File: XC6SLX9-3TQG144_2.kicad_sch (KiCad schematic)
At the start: 28 parts, among them U1 XC6SLX9-3TQG144

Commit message: updated design - still needs vcc routing
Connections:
- net GND: now also U1.108 (GND), U1.113 (GND), U1.13 (GND), U1.130 (GND), U1.136 (GND), U1.25 (GND), U1.3 (GND), U1.49 (GND), U1.54 (GND), U1.68 (GND), U1.73 (SUSPEND), U1.77 (GND), U1.91 (GND), U1.96 (GND); no longer U1.P108 (GND), U1.P113 (GND), U1.P13 (GND), U1.P130 (GND), U1.P136 (GND), U1.P25 (GND), U1.P3 (GND), U1.P49 (GND), U1.P54 (GND), U1.P68 (GND), U1.P73 (SUSPEND), U1.P77 (GND), U1.P91 (GND), U1.P96 (GND)
- net SHUNTL: now also U1.128 (VCCINT), U1.19 (VCCINT), U1.28 (VCCINT), U1.52 (VCCINT), U1.89 (VCCINT); no longer U1.P128 (VCCINT), U1.P19 (VCCINT), U1.P28 (VCCINT), U1.P52 (VCCINT), U1.P89 (VCCINT)
- net TCK: now also U1.109 (TCK); no longer U1.P109 (TCK)
- net TDI: now also U1.110 (TDI); no longer U1.P110 (TDI)
- net TDO: now also U1.106 (TDO); no longer U1.P106 (TDO)
- net TMS: now also U1.107 (TMS); no longer U1.P107 (TMS)
- net VCC: now also U1.103 (VCCO_1), U1.122 (VCCO_0), U1.125 (VCCO_0), U1.129 (VCCAUX), U1.135 (VCCO_0), U1.18 (VCCO_3), U1.20 (VCCAUX), U1.31 (VCCO_3), U1.36 (VCCAUX), U1.4 (VCCO_3), U1.42 (VCCO_2), U1.53 (VCCAUX), U1.63 (VCCO_2), U1.76 (VCCO_1), U1.86 (VCCO_1), U1.90 (VCCAUX); no longer U1.P103 (VCCO_1), U1.P122 (VCCO_0), U1.P125 (VCCO_0), U1.P129 (VCCAUX), U1.P135 (VCCO_0), U1.P18 (VCCO_3), U1.P20 (VCCAUX), U1.P31 (VCCO_3), U1.P36 (VCCAUX), U1.P4 (VCCO_3), U1.P42 (VCCO_2), U1.P53 (VCCAUX), U1.P63 (VCCO_2), U1.P76 (VCCO_1), U1.P86 (VCCO_1), U1.P90 (VCCAUX)
- net at R4.1, SJ2.2: now also U1.37 (PROGRAM_B_2); no longer U1.P37 (PROGRAM_B_2)
- net at D1.1, R5.1, SJ1.2: now also U1.71 (DONE_2); no longer U1.P71 (DONE_2)

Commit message: updated schematic and pcb, fixed silkscreen - Ready for review
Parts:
- renumbered SJ1 to JP1, SJ2 to JP2
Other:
- moved on the sheet: C1, C13, C14, C15, C16, C18, C19, C2, C20, C21, C3, C4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

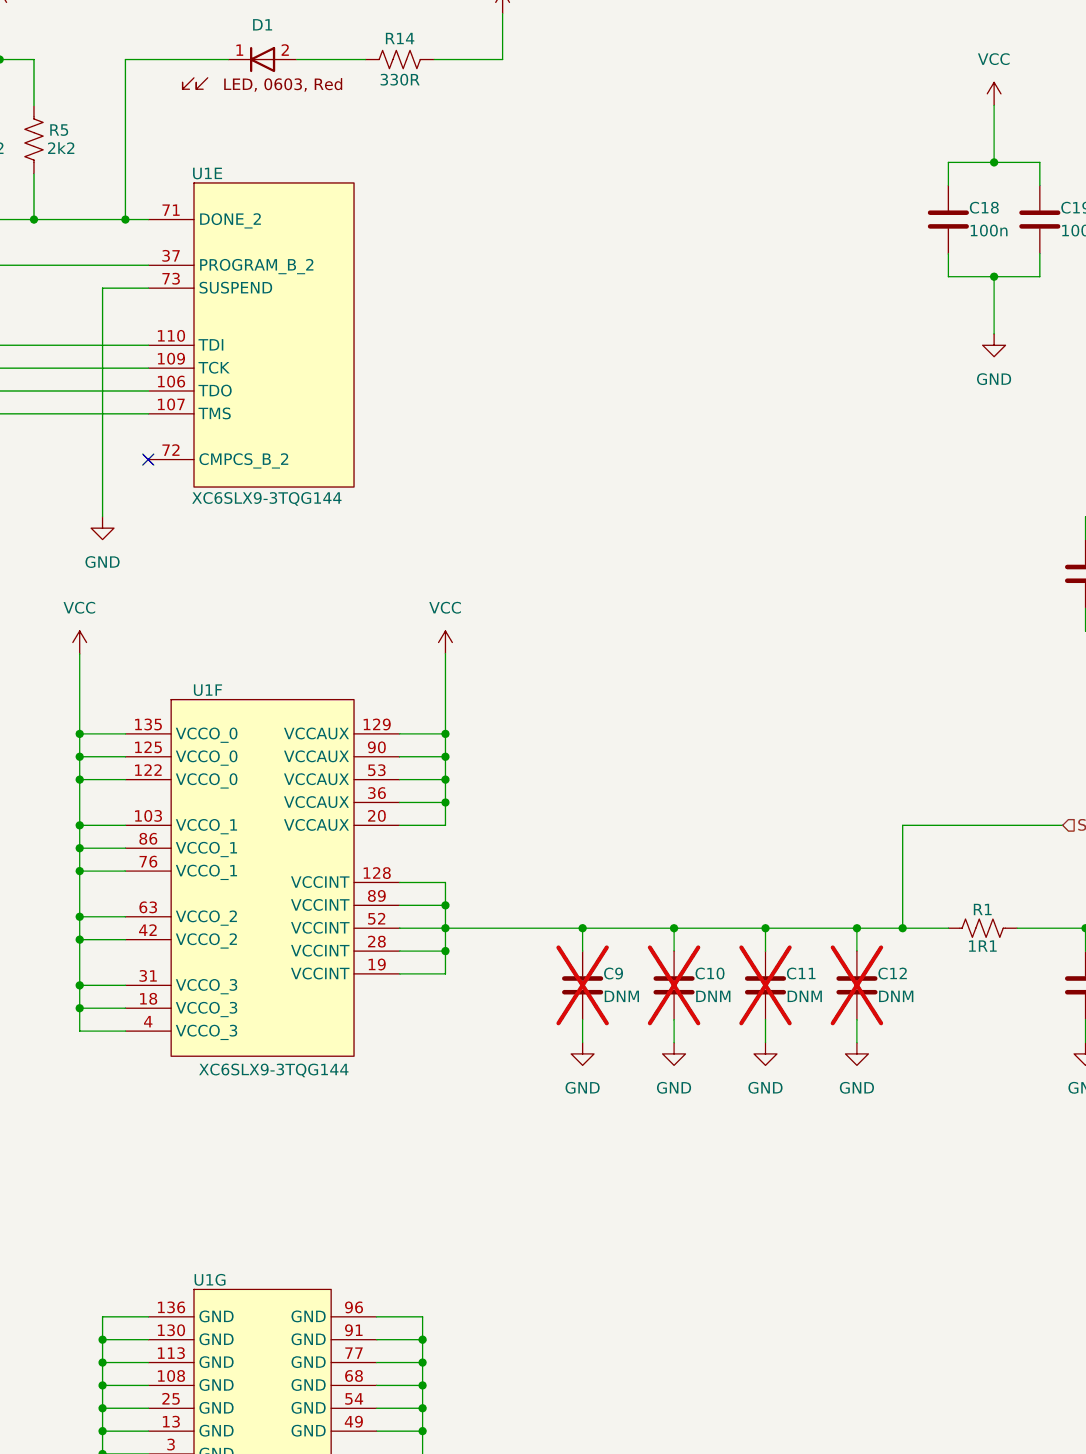
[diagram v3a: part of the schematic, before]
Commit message: updated schematic and pcb after library re-organization
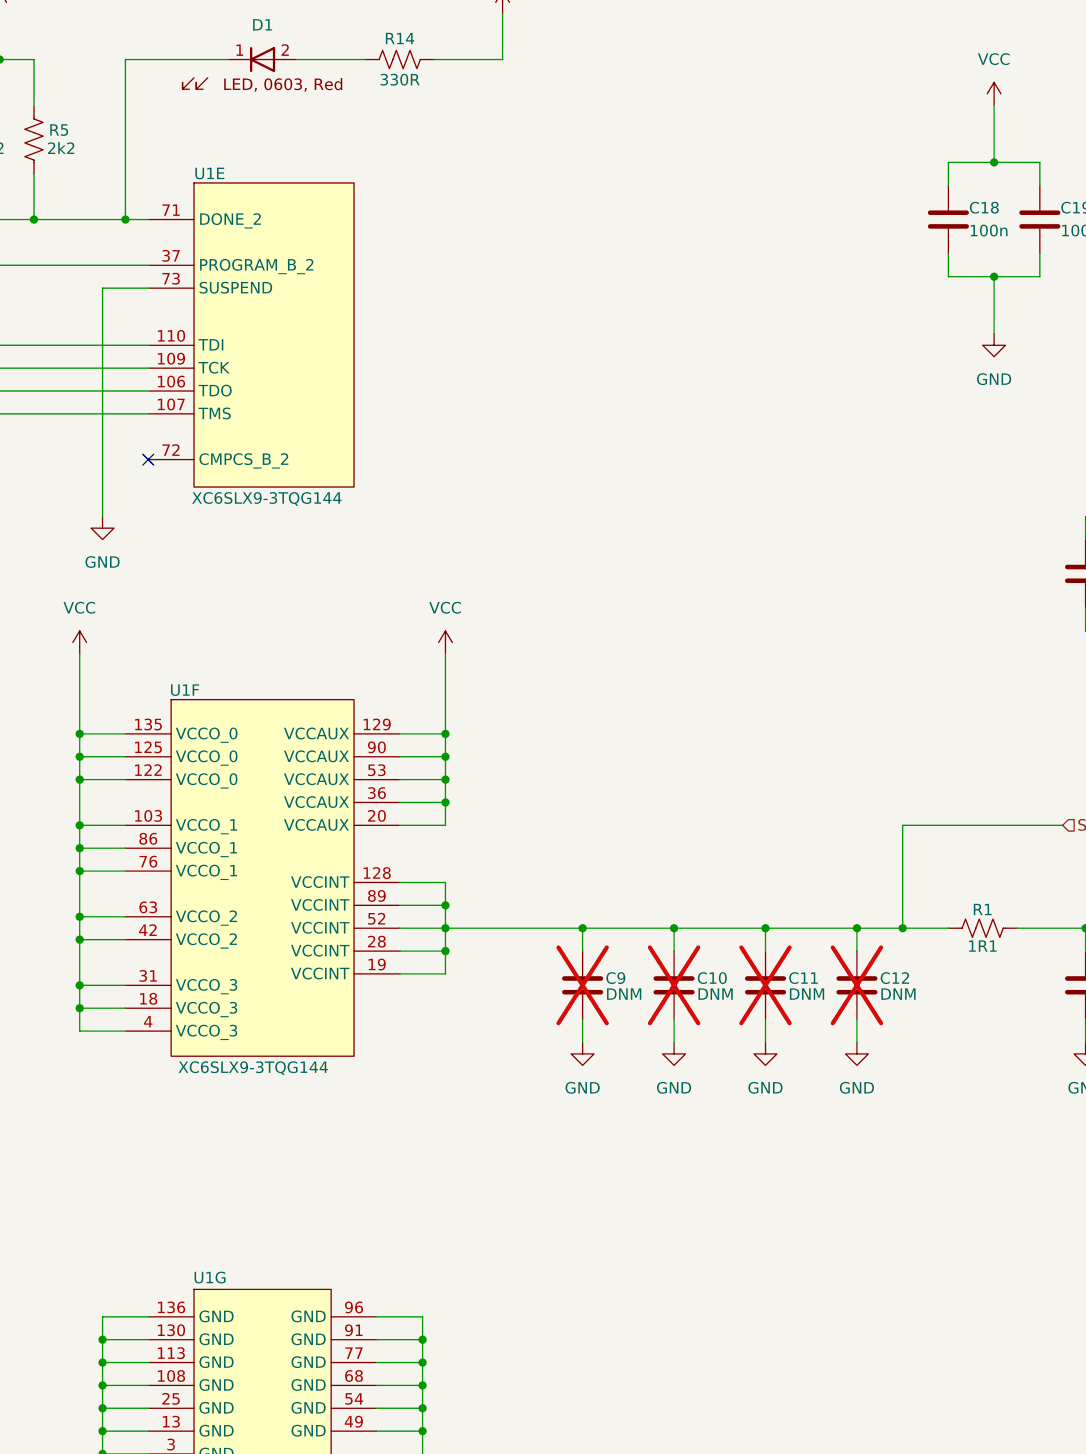
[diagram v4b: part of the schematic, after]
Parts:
- removed C10, C11, C12, C9: DNM_CAP_0603, Capacitor_SMD:C_0603_1608Metric, symbol tutorial_2_library:DNM_0603_cap
- removed U1: XC6SLX9-3TQG144, Package_QFP:TQFP-144_20x20mm_P0.5mm, symbol tutorial_2_library:XC6SLX9-3TQG144
- added C10, C11, C12, C9: DNM_CAP_0603, Capacitor_SMD:C_0603_1608Metric, symbol nae_caps:CAP_DNM_0603
- added U1: XC6SLX9-3TQG144, Package_QFP:TQFP-144_20x20mm_P0.5mm, symbol Integrated_Circuits:XC6SLX9-3TQG144
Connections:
- net GND: now also C10.1, C11.1, C12.1, C9.1, U1.108 (GND), U1.113 (GND), U1.13 (GND), U1.130 (GND), U1.136 (GND), U1.25 (GND), U1.3 (GND), U1.49 (GND), U1.54 (GND), U1.68 (GND), U1.73 (SUSPEND), U1.77 (GND), U1.91 (GND), U1.96 (GND)
- net SHUNTL: now also C10.2, C11.2, C12.2, C9.2, U1.128 (VCCINT), U1.19 (VCCINT), U1.28 (VCCINT), U1.52 (VCCINT), U1.89 (VCCINT)
- net TCK: now also U1.109 (TCK)
- net TDI: now also U1.110 (TDI)
- net TDO: now also U1.106 (TDO)
- net TMS: now also U1.107 (TMS)
- net VCC: now also U1.103 (VCCO_1), U1.122 (VCCO_0), U1.125 (VCCO_0), U1.129 (VCCAUX), U1.135 (VCCO_0), U1.18 (VCCO_3), U1.20 (VCCAUX), U1.31 (VCCO_3), U1.36 (VCCAUX), U1.4 (VCCO_3), U1.42 (VCCO_2), U1.53 (VCCAUX), U1.63 (VCCO_2), U1.76 (VCCO_1), U1.86 (VCCO_1), U1.90 (VCCAUX)
- net at JP2.2, R4.1: now also U1.37 (PROGRAM_B_2)
- net at D1.1, JP1.2, R5.1: now also U1.71 (DONE_2)

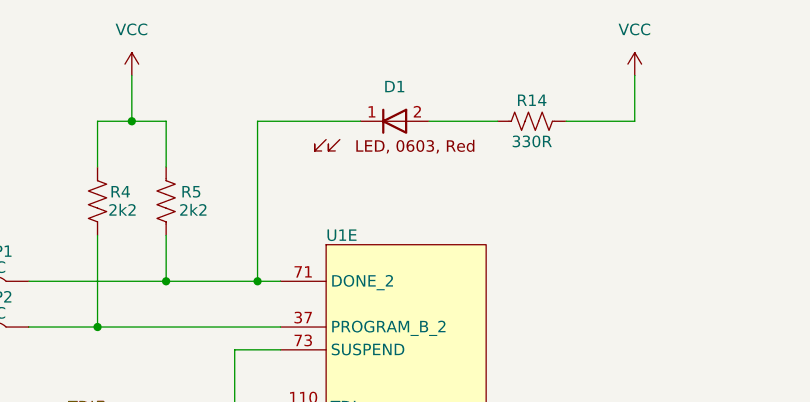
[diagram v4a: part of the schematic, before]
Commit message: updated pcb and schematic after library re-organization
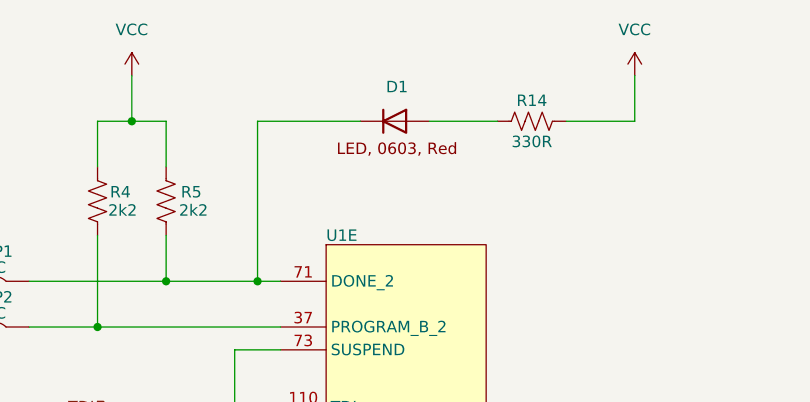
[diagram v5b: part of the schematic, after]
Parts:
- removed D1: APT1608SRCPRV, LED_SMD:LED_0603_1608Metric, symbol tutorial_2_library:APT1608SRCPRV
- added D1: APT1608SRCPRV, LED_SMD:LED_0603_1608Metric, symbol NAE_Diodes:APT1608SRCPRV_Red
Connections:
- net at JP1.2, R5.1, U1.71 (DONE_2): now also D1.1
- net at R14.1: now also D1.2
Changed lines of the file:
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@@
+	)
+	(symbol
+		(lib_id "NAE_Diodes:APT1608SRCPRV_Red")
+		(at 88.9 27.94 0)
+		(unit 1)
+		(exclude_from_sim no)
+		(in_bom yes)
+		(on_board yes)
+		(dnp no)
+		(fields_autoplaced yes)
+		(property "Reference" "D1"
+			(at 89.154 24.13 0)
+			(effects
+				(font
+					(size 1.27 1.27)
+				)
+			)
+		)
+		(property "Value" "APT1608SRCPRV"
+			(at 99.06 48.768 0)
+			(effects
+				(font
+					(size 1.27 1.27)
+				)
+				(hide yes)
+			)
+		)
+		(property "Footprint" "LED_SMD:LED_0603_1608Metric"
+			(at 89.408 45.72 0)
+			(effects
+				(font
+					(size 1.27 1.27)
+				)
+				(hide yes)
+			)
+		)
+		(property "Datasheet" "https://www.kingbrightusa.com/images/catalog/SPEC/APT1608SRCPRV.pdf"
+			(at 98.806 41.148 0)
+			(effects
+				(font
+					(size 1.27 1.27)
+				)
+				(hide yes)
+			)
+		)
+		(property "Description" "LED RED CLEAR CHIP SMD"
+			(at 88.646 38.608 0)
+			(effects
+				(font
+					(size 1.27 1.27)
+				)
+				(hide yes)
+			)
+		)
+		(property "Display Value" "APT1608SRCPRV"
+			(at 88.9 35.306 0)
+			(effects
+				(font
+					(size 1.27 1.27)
+				)
+				(hide yes)
+			)
+		)
+		(property "Manufacturer" "Kingbright"
+			(at 78.74 48.768 0)
+			(effects
+				(font
+					(size 1.27 1.27)
+				)
+				(hide yes)
+			)
+		)
+		(property "Manufacturer Part Number" "APT1608SRCPRV"
+			(at 88.646 43.434 0)
+			(effects
+				(font
+					(size 1.27 1.27)
+				)
+				(hide yes)
+			)
+		)
+		(property "Supplier 1" "DigiKey"
+			(at 72.39 51.308 0)
+			(effects
+				(font
+					(size 1.27 1.27)
+				)
+				(hide yes)
+			)
+		)
+		(property "Supplier 1 Part Number" "754-1122-1-ND"
+			(at 100.33 51.308 0)
+			(effects
+				(font
+					(size 1.27 1.27)
+				)
+				(hide yes)
+			)
+		)
+		(property "Supplier 2" ""
+			(at 88.9 27.94 0)
+			(effects
+				(font
+					(size 1.27 1.27)
+				)
+				(hide yes)
+			)
+		)
+		(property "Supplier 2 Part Number" ""
+			(at 88.9 27.94 0)
+			(effects
+				(font
+					(size 1.27 1.27)
+				)
+				(hide yes)
+			)
+		)
+		(pin "1"
+		)
+		(pin "2"
+		)
+		(instances
+			(project ""
+				(path "/06b23300-1735-453c-a53d-6066ed551221/d67991ef-1465-46d9-b7d2-47fb63c81bd9"
+					(reference "D1")
+					(unit 1)
+				)
+			)
+		)
 	)
 	(symbol
@@
 					(unit 1)
 				)
-			)
-		)
-	)
-	(symbol
-		(lib_id "tutorial_2_library:APT1608SRCPRV")
-		(at 88.9 27.94 0)
-		(unit 1)
-		(exclude_from_sim no)
-		(in_bom yes)
-		(on_board yes)
-		(dnp no)
-		(fields_autoplaced yes)
-		(property "Reference" "D1"
-			(at 88.9 24.13 0)
-			(effects
-				(font
-					(size 1.27 1.27)
-				)
-			)
-		)
-		(property "Value" "APT1608SRCPRV"
-			(at 98.806 44.196 0)
-			(effects
-				(font
-					(size 1.27 1.27)
-				)
-				(hide yes)
-			)
-		)
-		(property "Footprint" "LED_SMD:LED_0603_1608Metric"
-			(at 89.154 41.148 0)
-			(effects
-				(font
-					(size 1.27 1.27)
-				)
-				(hide yes)
-			)
-		)
-		(property "Datasheet" "https://www.kingbrightusa.com/images/catalog/SPEC/APT1608SRCPRV.pdf"
-			(at 98.552 36.576 0)
-			(effects
-				(font
-					(size 1.27 1.27)
-				)
-				(hide yes)
-			)
-		)
-		(property "Description" "LED RED CLEAR CHIP SMD"
-			(at 88.392 34.036 0)
-			(effects
-				(font
-					(size 1.27 1.27)
-				)
-				(hide yes)
-			)
-		)
-		(property "Display Value" "APT1608SRCPRV"
-			(at 88.646 30.734 0)
-			(effects
-				(font
-					(size 1.27 1.27)
-				)
-				(hide yes)
-			)
-		)
-		(property "Manufacturer" "Kingbright"
-			(at 78.486 44.196 0)
-			(effects
-				(font
-					(size 1.27 1.27)
-				)
-				(hide yes)
-			)
-		)
-		(property "Manufacturer Part Number" "APT1608SRCPRV"
-			(at 88.392 38.862 0)
-			(effects
-				(font
-					(size 1.27 1.27)
-				)
-				(hide yes)
-			)
-		)
-		(property "Supplier 1" "DigiKey"
-			(at 72.136 46.736 0)
-			(effects
-				(font
-					(size 1.27 1.27)
-				)
-				(hide yes)
-			)
-		)
-		(property "Supplier 1 Part Number" "754-1122-1-ND"
-			(at 100.076 46.736 0)
-			(effects
-				(font
-					(size 1.27 1.27)
-				)
-				(hide yes)
-			)
-		)
-		(property "Supplier 2" ""
-			(at 88.9 27.94 0)
-			(effects
-				(font
-					(size 1.27 1.27)
-				)
-				(hide yes)
-			)
-		)
-		(property "Supplier 2 Part Number" ""
-			(at 88.9 27.94 0)
-			(effects
-				(font
-					(size 1.27 1.27)
-				)
-				(hide yes)
-			)
-		)
-		(pin "1"
-		)
-		(pin "2"
-		)
-		(instances
-			(project ""
-				(path "/06b23300-1735-453c-a53d-6066ed551221/d67991ef-1465-46d9-b7d2-47fb63c81bd9"
-					(reference "D1")
-					(unit 1)
-				)
